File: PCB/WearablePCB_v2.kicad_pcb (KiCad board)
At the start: 2 copper layers, 84 parts, among them IC1 TMP117AIDRVR, J1 702461001, J2 Conn_02x02_Counter_Clockwise, Q1 NX138AKSX, U1 AGLN250V5-CSG81I, U10 NINA-B306-00B, U2 ADPD6000BCBZR7, U3 TPS61071DDCR, U4 TPS61071DDCR, U5 TPS73215MDBVREP, U6 TPS7A2018PDBVR, U7 TPS7A2018PDBVR, U8 TPS7A2033PDBVR, U9 ADP7118AUJZ-R7, Y1 SIT9003AC-23-18EB-24.000000T

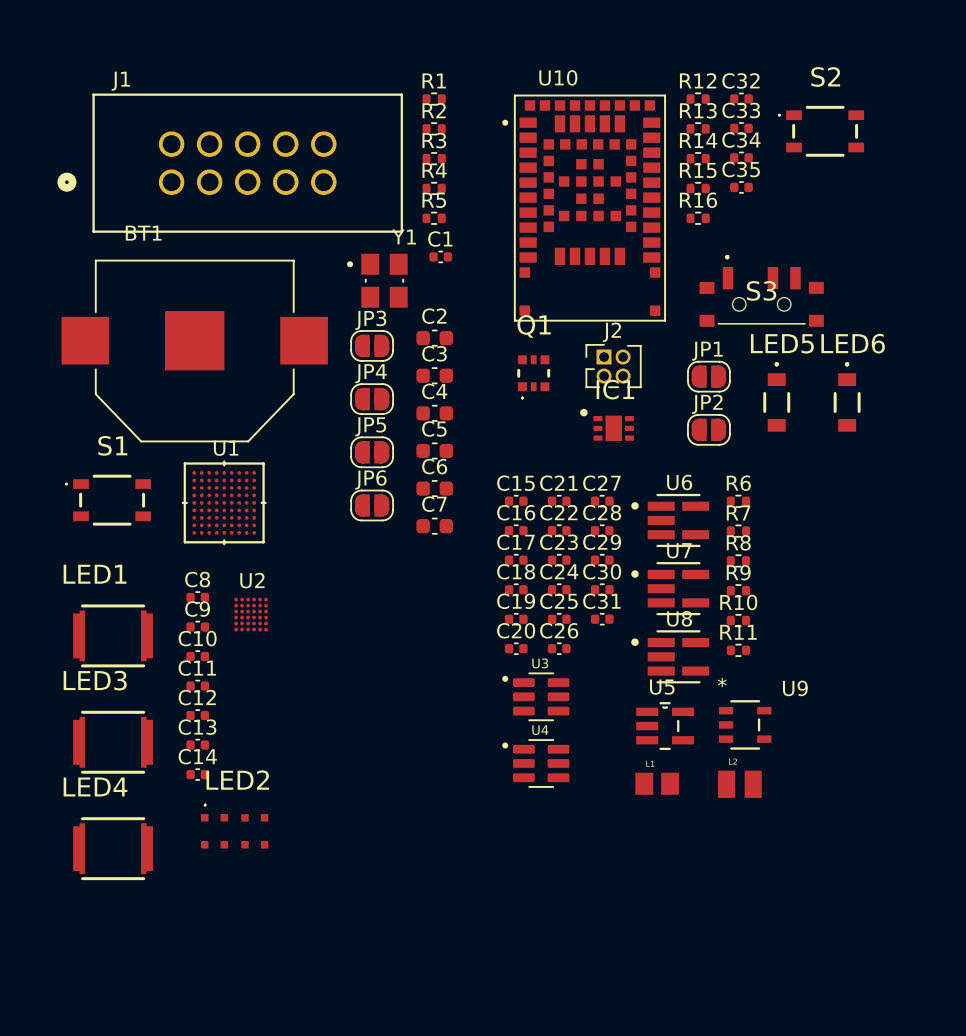
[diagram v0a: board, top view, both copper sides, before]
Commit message: Se adicionan PCB secundario para prototipado y también PCB con board-to-board connector
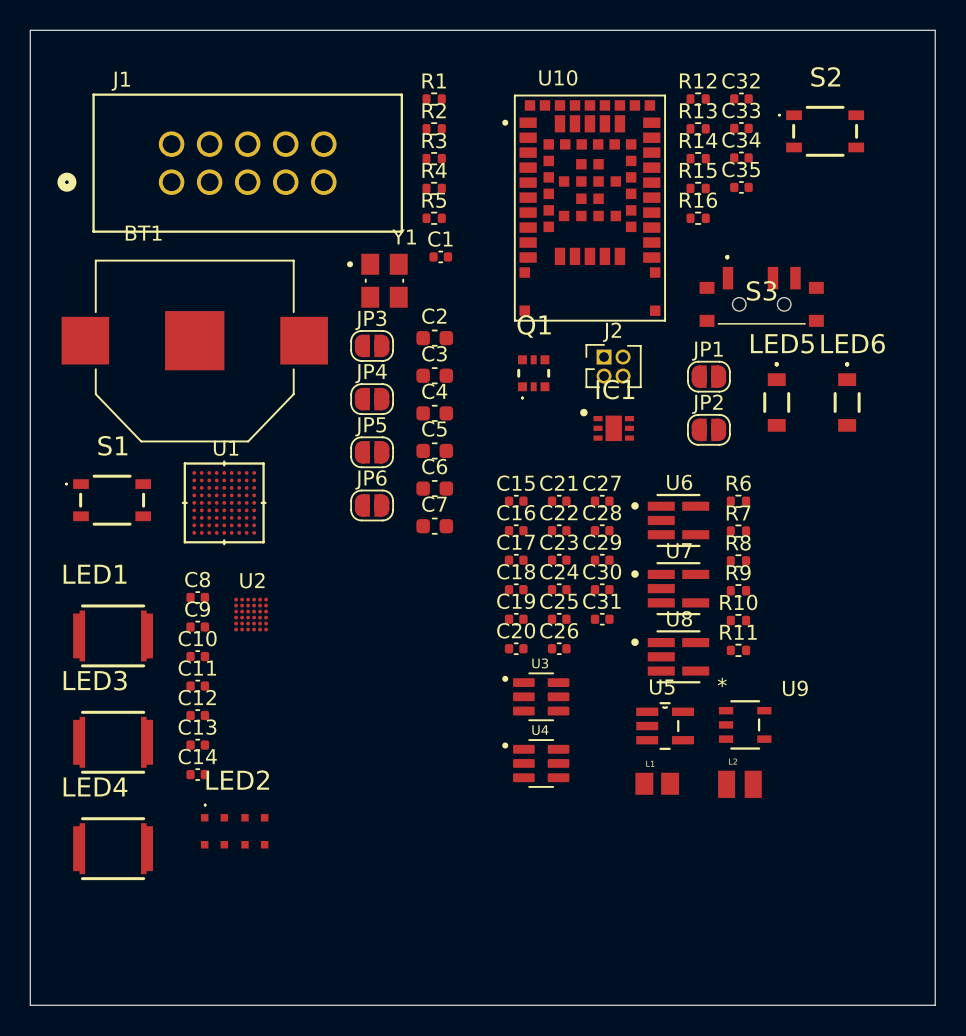
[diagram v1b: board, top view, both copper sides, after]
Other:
- board outline added: 60.4 x 65.1 mm
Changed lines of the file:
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@@
 		)
+	)
+	(gr_rect
+		(start 118.95582 68.53936)
+		(end 179.35448 133.61416)
+		(stroke
+			(width 0.05)
+			(type default)
+		)
+		(fill no)
+		(layer "Edge.Cuts")
 	)
 	(embedded_fonts no)
